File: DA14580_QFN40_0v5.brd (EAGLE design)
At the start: 92 x 73 mm, 29 parts, among them CON1 CON_TC2030-CTL-NL, IC1 1265-1137-1-ND, IC2 NC7SZ00M5XCT-ND, IC3 IC_LDO_XX1117_5, Q1 728-1076-1-ND, Q2 887-1833-1-ND, U1 DA14583-AT2, X1 SSW-114-02-S-S, X2 SSW-114-02-S-S

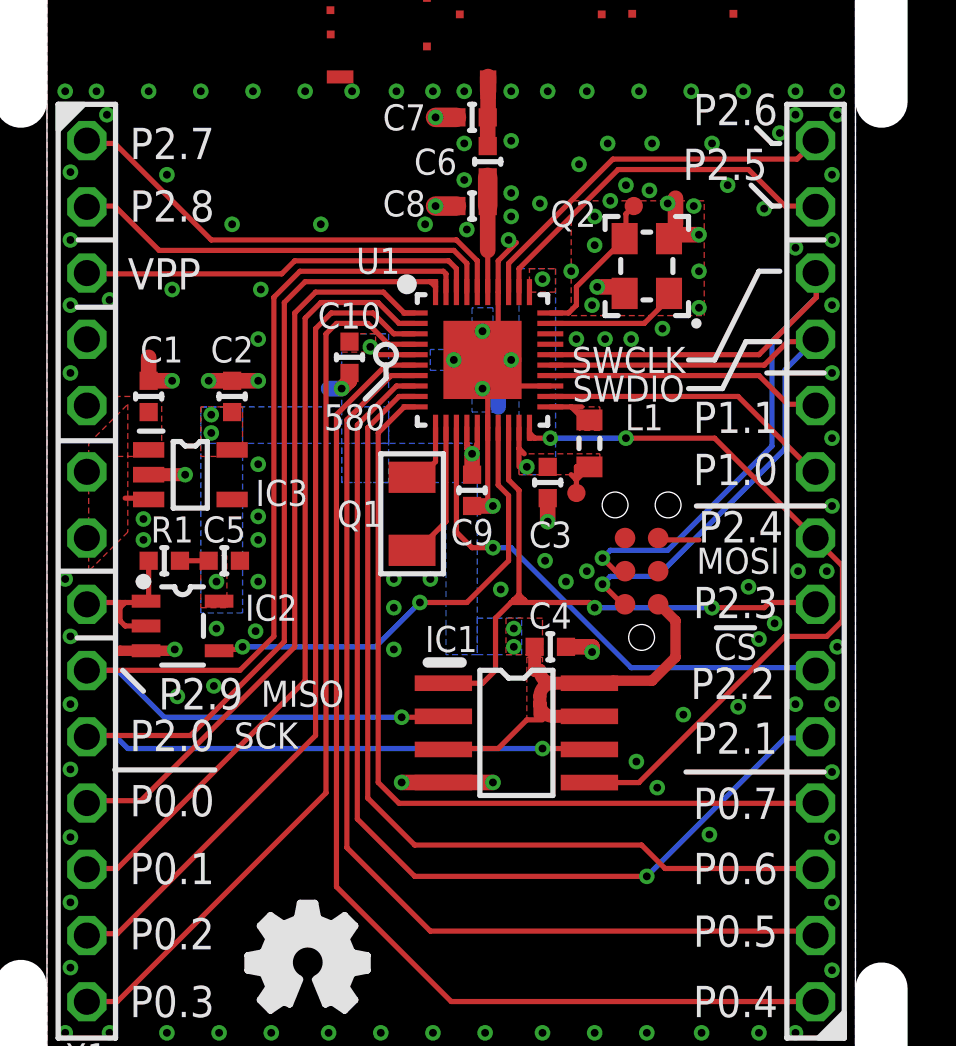
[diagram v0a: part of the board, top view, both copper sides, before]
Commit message: update eagle version: 7.5.0; library update
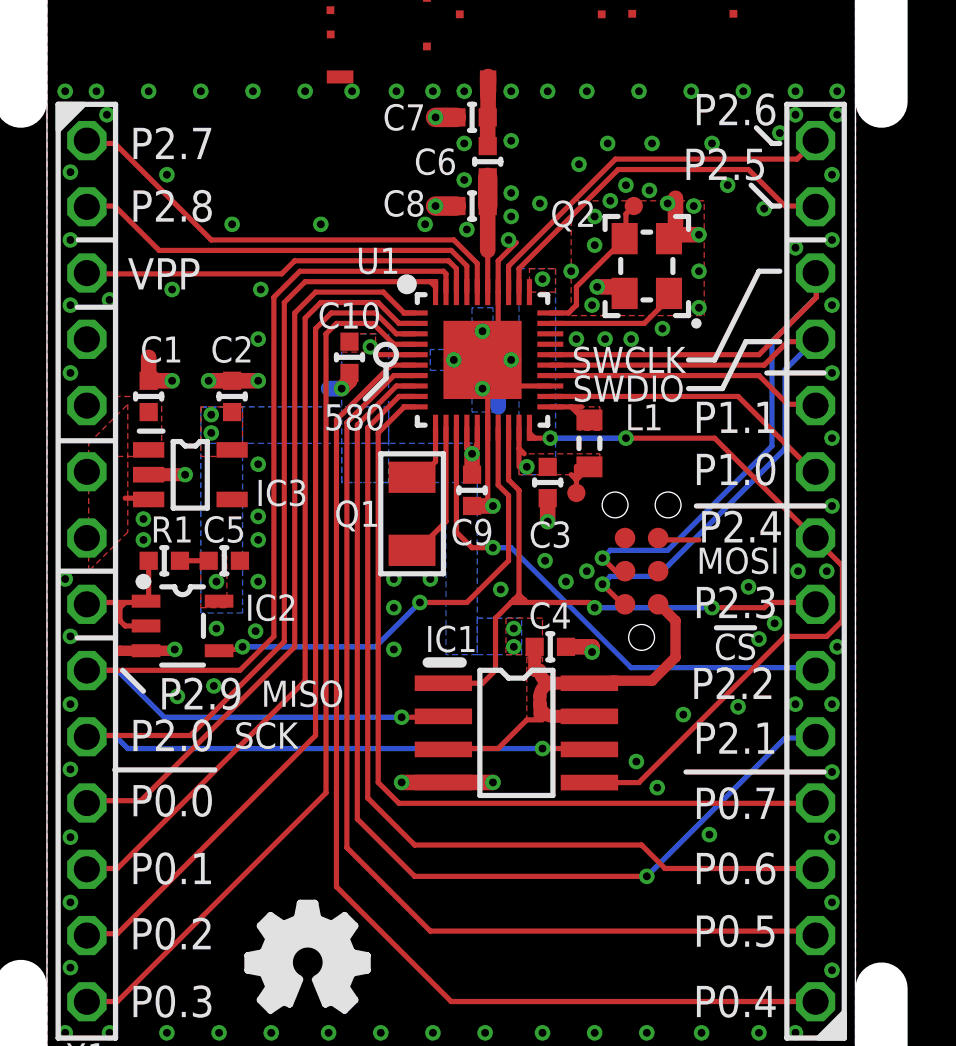
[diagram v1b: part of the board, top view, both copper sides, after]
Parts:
- IC1: value 1265-1137-1-ND -> IC_MEMORY_8P_AT25XE011_SOP
- IC3: value IC_LDO_XX1117_5 -> LDO5_3.3_SOT23
- Q2: value 887-1833-1-ND -> 16M_2520
- U1: value DA14583-AT2 -> DA14583AT2
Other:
- board text removed: "01-16"
- board text removed: "01-20"
- board text removed: "LAYER-STACK"

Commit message: [ 58x ] IC1 - tCream; add a selecter (580 or 583)
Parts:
- removed TP6: TPPAD1-13, testpad_local:P1-13
- added TP91: TESTPAD_F, mylib:FIDUCIAL
- C7, C8: value (none) -> NM
- Q1: value 728-1076-1-ND -> 32.768k
- Q2: value 16M_2520 -> 16M/2520
- TP1: value TPTP07R -> TESTPAD; device testpad_local:TP07R -> mylib:TP06RECT
- TP2: value TESTPAD_F -> TESTPAD; device mylib:FIDUCIAL -> mylib:TP06RECT
- TP3: value TPTP07R -> TPPAD1-13; device testpad_local:TP07R -> testpad_local:P1-13
- moved TP3 35.5 mm to (32.6, 13.5)
- moved TP2 25.8 mm to (32.5, 49.0), turned to 90 degrees
- moved TP1 0.10 mm to (30.3, 37.9)
- renumbered TP4 to TP92, TP5 to TP93
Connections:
- net GND: now also TP3.TP; no longer TP6.TP
- net N$21: now also TP2.TP; no longer TP3.TP
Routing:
- net VCC: track 23.3 -> 24.7 mm
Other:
- board text added: "DA14583-AT2 DA14580-AT2"
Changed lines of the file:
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@@
 <layer number="20" name="Dimension" color="15" fill="1" visible="yes" active="yes"/>
 <layer number="21" name="tPlace" color="7" fill="1" visible="yes" active="yes"/>
-<layer number="22" name="bPlace" color="7" fill="1" visible="no" active="yes"/>
+<layer number="22" name="bPlace" color="7" fill="1" visible="yes" active="yes"/>
 <layer number="23" name="tOrigins" color="15" fill="1" visible="yes" active="yes"/>
 <layer number="24" name="bOrigins" color="15" fill="1" visible="yes" active="yes"/>
-<layer number="25" name="tNames" color="7" fill="1" visible="yes" active="yes"/>
+<layer number="25" name="tNames" color="7" fill="1" visible="no" active="yes"/>
 <layer number="26" name="bNames" color="7" fill="1" visible="no" active="yes"/>
 <layer number="27" name="tValues" color="7" fill="1" visible="no" active="yes"/>
@@
 <vertex x="30.2" y="39.6"/>
 </polygon>
-<wire x1="28" y1="45.1" x2="28.4" y2="44.7" width="0" layer="42"/>
-<wire x1="28.4" y1="44.7" x2="28.4" y2="41.5" width="0" layer="42"/>
-<wire x1="28.4" y1="41.5" x2="28" y2="41.1" width="0" layer="42"/>
 <polygon width="0.2" layer="41">
 <vertex x="31.5" y="48.6"/>
@@
 silks on top/bottom layers</text>
 <circle x="32.6" y="13.5" radius="1.6" width="0.2" layer="21"/>
+<text x="20.6" y="22.7" size="1.2" layer="21" ratio="17">DA14583-AT2
+DA14580-AT2</text>
+<polygon width="0.2" layer="21">
+<vertex x="19.4" y="25.6"/>
+<vertex x="20.2" y="25.6"/>
+<vertex x="20.2" y="24.6"/>
+<vertex x="19.4" y="24.6"/>
+</polygon>
+<polygon width="0.2" layer="21">
+<vertex x="19.4" y="23.8"/>
+<vertex x="20.2" y="23.8"/>
+<vertex x="20.2" y="22.8"/>
+<vertex x="19.4" y="22.8"/>
+</polygon>
 </plain>
 <attributes>
@@
 <attribute name="DIGIKEY" value="" x="26.7" y="43.1" size="1.778" layer="27" display="off"/>
 </element>
-<element name="Q1" library="mylib" package="CRYSTAL_FC-135" value="728-1076-1-ND" x="24" y="37.2" smashed="yes" rot="R90">
+<element name="Q1" library="mylib" package="CRYSTAL_FC-135" value="32.768k" x="24" y="37.2" smashed="yes" rot="R90">
 <attribute name="NAME" x="21.9" y="37.2" size="1" layer="25" font="vector" ratio="20" align="center"/>
 <attribute name="VALUE" x="26.15" y="36.175" size="1.27" layer="27" rot="R90"/>
@@
 <attribute name="DIGIKEY" value="490-3261-1-ND" x="29.3" y="32.1" size="1.778" layer="27" display="off"/>
 </element>
-<element name="TP1" library="testpad_local" package="TP07R" value="TPTP07R" x="30.3" y="38" smashed="yes">
-<attribute name="VALUE" x="29.792" y="37.365" size="0.0254" layer="27"/>
-</element>
 <element name="X1" library="con-samtec.local" package="SSW-114-02-S-S" value="SSW-114-02-S-S" x="11.53" y="35" smashed="yes" rot="R270">
 <attribute name="NAME" x="11.5" y="16.4" size="1" layer="25" font="vector" ratio="20" align="center"/>
@@
 <attribute name="DIGIKEY" value="490-3261-1-ND" x="16.8" y="35.4" size="1.778" layer="27" display="off"/>
 </element>
-<element name="TP3" library="testpad_local" package="TP07R" value="TPTP07R" x="32.5" y="49" smashed="yes">
-<attribute name="VALUE" x="31.992" y="48.365" size="0.0254" layer="27"/>
-</element>
 <element name="IC3" library="mylib" package="IC_05_0.95_50MIL" value="LDO5_3.3_SOT23" x="15.5" y="38.7" smashed="yes" rot="R270">
 <attribute name="NAME" x="19" y="38" size="1" layer="25" font="vector" ratio="20" align="center"/>
@@
 <attribute name="VALUE" x="11.4" y="35.4" size="1.27" layer="27" ratio="16" rot="R270"/>
 </element>
-<element name="TP6" library="testpad_local" package="P1-13" value="TPPAD1-13" x="32.6" y="13.5" smashed="yes">
+<element name="TP3" library="testpad_local" package="P1-13" value="TPPAD1-13" x="32.6" y="13.5" smashed="yes">
 <attribute name="VALUE" x="32.6" y="13.5" size="0.0254" layer="27"/>
 </element>
@@
 <attribute name="DIGIKEY" value="490-5921-1-ND" x="26.9" y="50.7" size="1.778" layer="27" rot="R90" display="off"/>
 </element>
-<element name="C7" library="mylib" package="C0402" value="" x="26.3" y="52.4" smashed="yes" rot="R180">
+<element name="C7" library="mylib" package="C0402" value="NM" x="26.3" y="52.4" smashed="yes" rot="R180">
 <attribute name="NAME" x="23.7" y="52.4" size="1" layer="25" font="vector" ratio="20" rot="R180" align="center"/>
 <attribute name="VALUE" x="26.9" y="54.3" size="1" layer="27" font="vector" ratio="20" rot="R180"/>
@@
 <attribute name="DIGIKEY" value="" x="26.3" y="52.4" size="1.778" layer="27" rot="R180" display="off"/>
 </element>
-<element name="C8" library="mylib" package="C0402" value="" x="26.3" y="49" smashed="yes" rot="R180">
+<element name="C8" library="mylib" package="C0402" value="NM" x="26.3" y="49" smashed="yes" rot="R180">
 <attribute name="NAME" x="23.7" y="49.1" size="1" layer="25" font="vector" ratio="20" rot="R180" align="center"/>
 <attribute name="VALUE" x="26.9" y="50.9" size="1" layer="27" font="vector" ratio="20" rot="R180"/>
@@
 <element name="CON1" library="mylib" package="CON_TC2030-IDC-NL" value="CON_TC2030-CTL-NL" x="32.8" y="35" rot="R90"/>
 <element name="U$2" library="mylib" package="ICON_OSHW" value="ICON_OSHW" x="20" y="20"/>
-<element name="Q2" library="mylib" package="CLOCK_2520" value="16M_2520" x="33" y="46.7" smashed="yes" rot="R90">
+<element name="Q2" library="mylib" package="CLOCK_2520" value="16M/2520" x="33" y="46.7" smashed="yes" rot="R90">
 <attribute name="NAME" x="29.3" y="48.2" size="1" layer="25" font="vector" ratio="20"/>
 <attribute name="AKIZUKI" value="" x="33" y="46.7" size="1.778" layer="27" rot="R90" display="off"/>
@@
 <attribute name="DIGIKEY" value="887-1833-1-ND" x="33" y="46.7" size="1.778" layer="27" rot="R90" display="off"/>
 </element>
-<element name="TP2" library="mylib" package="FIDUCIAL" value="TESTPAD_F" x="15" y="68"/>
-<element name="TP4" library="mylib" package="FIDUCIAL" value="TESTPAD_F" x="15" y="5"/>
-<element name="TP5" library="mylib" package="FIDUCIAL" value="TESTPAD_F" x="72" y="5"/>
+<element name="TP91" library="mylib" package="FIDUCIAL" value="TESTPAD_F" x="15" y="68"/>
+<element name="TP92" library="mylib" package="FIDUCIAL" value="TESTPAD_F" x="15" y="5"/>
+<element name="TP93" library="mylib" package="FIDUCIAL" value="TESTPAD_F" x="72" y="5"/>
+<element name="TP1" library="mylib" package="TP06RECT" value="TESTPAD" x="30.3" y="37.9" smashed="yes">
+<attribute name="VALUE" x="30.046" y="37.519" size="0.0254" layer="27"/>
+</element>
+<element name="TP2" library="mylib" package="TP06RECT" value="TESTPAD" x="32.5" y="49" smashed="yes" rot="R90">
+<attribute name="VALUE" x="32.881" y="48.746" size="0.0254" layer="27" rot="R90"/>
+</element>
 </elements>
 <signals>
@@
 <contactref element="IC2" pad="3"/>
 <contactref element="IC2" pad="3"/>
-<contactref element="TP6" pad="TP"/>
+<contactref element="TP3" pad="TP"/>
 <wire x1="29.3" y1="42.1" x2="27.7" y2="42.1" width="0.2" layer="1"/>
 <wire x1="26.7" y1="42" x2="26.9" y2="41.8" width="0.2" layer="1"/>
@@
 <signal name="N$21">
 <contactref element="U1" pad="30"/>
-<contactref element="TP3" pad="TP"/>
 <wire x1="29.3" y1="44.9" x2="30" y2="44.9" width="0.2" layer="1"/>
 <wire x1="30.3" y1="45.9" x2="32.15" y2="47.75" width="0.2" layer="1"/>
@@
 <wire x1="32.2" y1="48.7" x2="32.5" y2="49" width="0.2" layer="1"/>
 <contactref element="Q2" pad="3"/>
+<contactref element="TP2" pad="TP"/>
 </signal>
 <signal name="VCC">
@@
 <wire x1="28.7" y1="32.1" x2="28.7" y2="31.2" width="0.5" layer="1"/>
 <wire x1="28.7" y1="31.2" x2="28.9" y2="31.2" width="0.5" layer="1"/>
+<wire x1="23.3" y1="39.9" x2="23.1" y2="40.1" width="0.2" layer="16" curve="-90"/>
+<wire x1="21.1" y1="39.9" x2="21.3" y2="39.7" width="0.2" layer="16" curve="-90"/>
+<wire x1="17.5" y1="39.7" x2="17.7" y2="39.9" width="0.2" layer="16" curve="-90"/>
+<wire x1="25.1" y1="38.4" x2="25.3" y2="38.2" width="0.2" layer="16" curve="-90"/>
+<wire x1="26.7" y1="33.2" x2="26.5" y2="33.4" width="0.2" layer="16" curve="-90"/>
 </signal>
 <signal name="N$6">
@@
 <contactref element="C3" pad="1"/>
 <contactref element="L1" pad="1"/>
-<contactref element="TP1" pad="TP"/>
 <polygon width="0.2" layer="1" thermals="no">
 <vertex x="28.1" y="39.5"/>
@@
 <via x="28.4" y="39" extent="1-16" drill="0.3"/>
 <wire x1="28.1" y1="39.7" x2="28.1" y2="39" width="0.2" layer="1"/>
-<wire x1="30.3" y1="38" x2="30.3" y2="38.5" width="0.2" layer="1"/>
 <wire x1="30.3" y1="38.5" x2="30.3" y2="39" width="0.2" layer="1"/>
 <wire x1="30.3" y1="39" x2="30.8" y2="39" width="0.2" layer="1"/>
@@
 <wire x1="30.3" y1="38.5" x2="30.1" y2="38.7" width="0.2" layer="1"/>
 <wire x1="30.3" y1="38.5" x2="30.5" y2="38.7" width="0.2" layer="1"/>
+<contactref element="TP1" pad="TP"/>
+<wire x1="30.3" y1="38.5" x2="30.3" y2="37.9" width="0.2" layer="1"/>
 </signal>
 <signal name="!RESET!">

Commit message: [ 58x ] Q1 Digikey number replace
728-1076-1-ND  -> 1253-1342-1-ND
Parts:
- TP1, TP2: value TESTPAD -> (none)
- TP91, TP92, TP93: value TESTPAD_F -> (none)
- U$2: value ICON_OSHW -> (none)
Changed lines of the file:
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@@
 <attribute name="AKIZUKI" value="" x="24" y="37.2" size="1.778" layer="27" rot="R90" display="off"/>
 <attribute name="MOUSER" value="" x="24" y="37.2" size="1.778" layer="27" rot="R90" display="off"/>
-<attribute name="DIGIKEY" value="728-1076-1-ND" x="24" y="37.2" size="1.778" layer="27" rot="R90" display="off"/>
+<attribute name="DIGIKEY" value="1253-1342-1-ND" x="24" y="37.2" size="1.778" layer="27" rot="R90" display="off"/>
 </element>
 <element name="C1" library="mylib" package="C0402" value="" x="13.9" y="41.7" smashed="yes" rot="R90">
@@
 <element name="U$1" library="mylib" package="ANT_IFA_V2" value="ANT_IFA" x="26.9" y="53.7"/>
 <element name="CON1" library="mylib" package="CON_TC2030-IDC-NL" value="CON_TC2030-CTL-NL" x="32.8" y="35" rot="R90"/>
-<element name="U$2" library="mylib" package="ICON_OSHW" value="ICON_OSHW" x="20" y="20"/>
+<element name="U$2" library="mylib" package="ICON_OSHW" value="" x="20" y="20">
+<attribute name="NOT_COMPONENT" value="YES" x="20" y="20" size="1.778" layer="27" display="off"/>
+</element>
 <element name="Q2" library="mylib" package="CLOCK_2520" value="16M/2520" x="33" y="46.7" smashed="yes" rot="R90">
 <attribute name="NAME" x="29.3" y="48.2" size="1" layer="25" font="vector" ratio="20"/>
@@
 <attribute name="DIGIKEY" value="887-1833-1-ND" x="33" y="46.7" size="1.778" layer="27" rot="R90" display="off"/>
 </element>
-<element name="TP91" library="mylib" package="FIDUCIAL" value="TESTPAD_F" x="15" y="68"/>
-<element name="TP92" library="mylib" package="FIDUCIAL" value="TESTPAD_F" x="15" y="5"/>
-<element name="TP93" library="mylib" package="FIDUCIAL" value="TESTPAD_F" x="72" y="5"/>
-<element name="TP1" library="mylib" package="TP06RECT" value="TESTPAD" x="30.3" y="37.9" smashed="yes">
+<element name="TP91" library="mylib" package="FIDUCIAL" value="" x="15" y="68">
+<attribute name="NOT_COMPONENT" value="YES" x="15" y="68" size="1.778" layer="27" display="off"/>
+</element>
+<element name="TP92" library="mylib" package="FIDUCIAL" value="" x="15" y="5">
+<attribute name="NOT_COMPONENT" value="YES" x="15" y="5" size="1.778" layer="27" display="off"/>
+</element>
+<element name="TP93" library="mylib" package="FIDUCIAL" value="" x="72" y="5">
+<attribute name="NOT_COMPONENT" value="YES" x="72" y="5" size="1.778" layer="27" display="off"/>
+</element>
+<element name="TP1" library="mylib" package="TP06RECT" value="" x="30.3" y="37.9" smashed="yes">
 <attribute name="VALUE" x="30.046" y="37.519" size="0.0254" layer="27"/>
+<attribute name="NOT_COMPONENT" value="YES" x="30.3" y="37.9" size="1.778" layer="27" display="off"/>
 </element>
-<element name="TP2" library="mylib" package="TP06RECT" value="TESTPAD" x="32.5" y="49" smashed="yes" rot="R90">
+<element name="TP2" library="mylib" package="TP06RECT" value="" x="32.5" y="49" smashed="yes" rot="R90">
 <attribute name="VALUE" x="32.881" y="48.746" size="0.0254" layer="27" rot="R90"/>
+<attribute name="NOT_COMPONENT" value="YES" x="32.5" y="49" size="1.778" layer="27" rot="R90" display="off"/>
 </element>
 </elements>

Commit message: [ 58x ] v0.5 frozen
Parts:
- added GIT1: 35b58a7, git-revision:GIT-REVISION
- added ICON1: v0.5, mylib:ICON_REVISION
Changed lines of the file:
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@@
 <attribute name="VALUE" x="26.15" y="36.175" size="1.27" layer="27" rot="R90"/>
 <attribute name="AKIZUKI" value="" x="24" y="37.2" size="1.778" layer="27" rot="R90" display="off"/>
-<attribute name="MOUSER" value="" x="24" y="37.2" size="1.778" layer="27" rot="R90" display="off"/>
-<attribute name="DIGIKEY" value="1253-1342-1-ND" x="24" y="37.2" size="1.778" layer="27" rot="R90" display="off"/>
+<attribute name="MOUSER" value="732-FC135-32.76KAAG" x="24" y="37.2" size="1.778" layer="27" rot="R90" display="off"/>
+<attribute name="DIGIKEY" value="" x="24" y="37.2" size="1.778" layer="27" rot="R90" display="off"/>
 </element>
 <element name="C1" library="mylib" package="C0402" value="" x="13.9" y="41.7" smashed="yes" rot="R90">
@@
 <attribute name="NOT_COMPONENT" value="YES" x="32.5" y="49" size="1.778" layer="27" rot="R90" display="off"/>
 </element>
+<element name="GIT1" library="git-revision" package="GIT-REVISION" value="35b58a7" x="-6.4" y="-13.5"/>
+<element name="ICON1" library="mylib" package="ICON_REVISION" value="v0.5" x="-1.2" y="-16.2">
+<attribute name="NOT_COMPONENT" value="YES" x="-1.2" y="-16.2" size="1.778" layer="27" display="off"/>
+</element>
 </elements>
